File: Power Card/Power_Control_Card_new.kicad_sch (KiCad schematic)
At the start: 20 parts, among them J4 Conn_01x04_Pin, Q1 IRF5305PbF, Q2 IRF5305PbF, U3 TSR2-2450, U4 TSR2-2433, U5 MCP9808_MSOP

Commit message: test msg
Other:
- note removed: "PRETTY PLEASE SAVE (this is a git test)"
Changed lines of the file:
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@@
-		)
-	)
-	(text "PRETTY PLEASE SAVE (this is a git test)"
-		(exclude_from_sim no)
-		(at 36.068 17.018 0)
-		(effects
-			(font
-				(size 1.27 1.27)
-			)
 		)
 	)

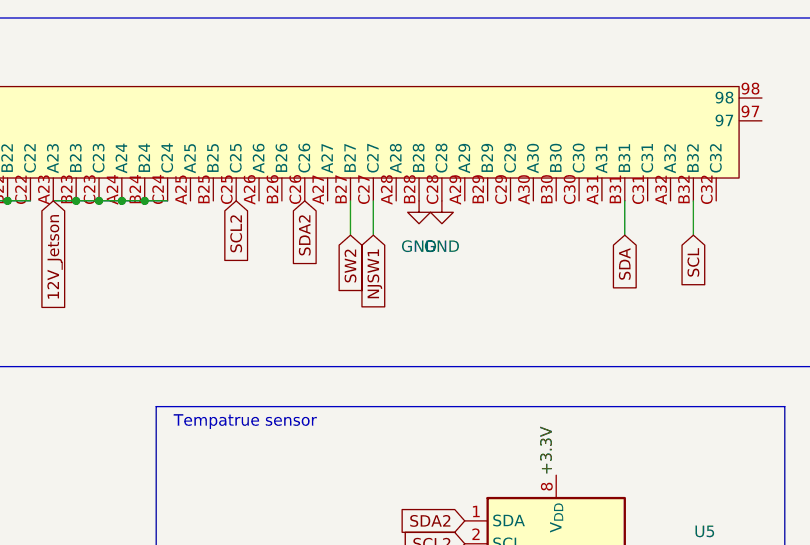
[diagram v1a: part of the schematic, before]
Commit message: Changed Backplane and Power Card for proper connection between the killswitches in the new system
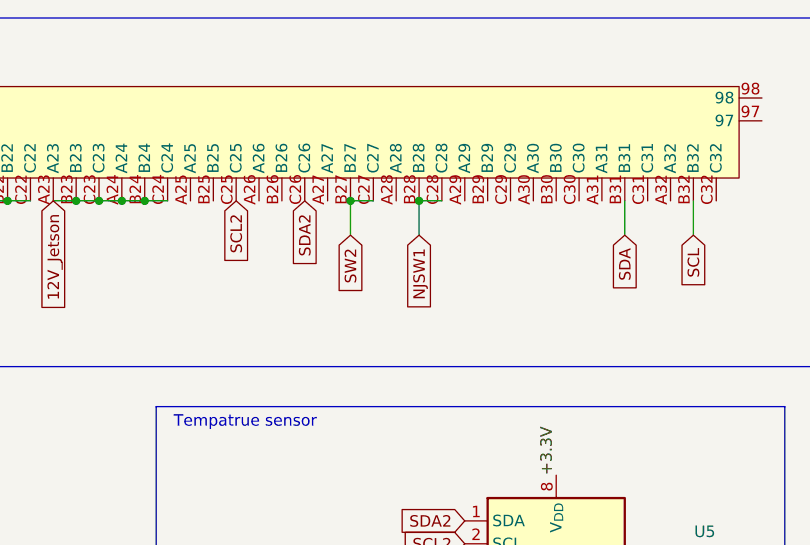
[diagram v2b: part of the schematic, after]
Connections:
- net GND: no longer J2.B28, J2.C28
- net NJSW1: now also J2.B28, J2.C28; no longer J2.C27
- net SW2: now also J2.C27
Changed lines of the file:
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@@
 	)
 	(junction
+		(at 270.51 91.44)
+		(diameter 0)
+		(color 0 0 0 0)
+	)
+	(junction
 		(at 146.05 91.44)
 		(diameter 0)
@@
 	)
 	(junction
+		(at 262.89 91.44)
+		(diameter 0)
+		(color 0 0 0 0)
+	)
+	(junction
 		(at 83.82 149.86)
 		(diameter 0)
@@
 	(wire
 		(pts
+			(xy 270.51 91.44) (xy 273.05 91.44)
+		)
+		(stroke
+			(width 0)
+			(type default)
+		)
+	)
+	(wire
+		(pts
 			(xy 118.11 91.44) (xy 120.65 91.44)
 		)
@@
 	(wire
 		(pts
-			(xy 152.4 177.8) (xy 152.4 173.99)
+			(xy 262.89 91.44) (xy 265.43 91.44)
 		)
 		(stroke
@@
 	(wire
 		(pts
-			(xy 82.55 91.44) (xy 85.09 91.44)
+			(xy 152.4 177.8) (xy 152.4 173.99)
 		)
 		(stroke
@@
 	(wire
 		(pts
-			(xy 176.53 91.44) (xy 179.07 91.44)
+			(xy 82.55 91.44) (xy 85.09 91.44)
 		)
 		(stroke
@@
 	(wire
 		(pts
-			(xy 107.95 91.44) (xy 110.49 91.44)
+			(xy 176.53 91.44) (xy 179.07 91.44)
 		)
 		(stroke
@@
 	(wire
 		(pts
-			(xy 152.4 185.42) (xy 152.4 195.58)
+			(xy 107.95 91.44) (xy 110.49 91.44)
 		)
 		(stroke
@@
 	(wire
 		(pts
-			(xy 170.18 133.35) (xy 172.72 133.35)
+			(xy 152.4 185.42) (xy 152.4 195.58)
 		)
 		(stroke
@@
 	(wire
 		(pts
-			(xy 265.43 91.44) (xy 265.43 95.25)
+			(xy 170.18 133.35) (xy 172.72 133.35)
 		)
 		(stroke
@@
 	(wire
 		(pts
+			(xy 270.51 91.44) (xy 270.51 95.25)
+		)
+		(stroke
+			(width 0)
+			(type default)
+		)
+	)
+	(wire
+		(pts
 			(xy 179.07 91.44) (xy 181.61 91.44)
 		)
@@
 	(global_label "NJSW1"
 		(shape input)
-		(at 265.43 95.25 270)
+		(at 270.51 95.25 270)
 		(fields_autoplaced yes)
 		(effects
@@
 		)
 		(property "Intersheetrefs" "${INTERSHEET_REFS}"
-			(at 265.43 104.4037 90)
+			(at 270.51 104.4037 90)
 			(effects
 				(font
@@
 	)
 	(symbol
-		(lib_name "GND_1")
-		(lib_id "power:GND")
-		(at 273.05 91.44 0)
-		(unit 1)
-		(exclude_from_sim no)
-		(in_bom yes)
-		(on_board yes)
-		(dnp no)
-		(fields_autoplaced yes)
-		(property "Reference" "#PWR011"
-			(at 273.05 97.79 0)
-			(effects
-				(font
-					(size 1.27 1.27)
-				)
-				(hide yes)
-			)
-		)
-		(property "Value" "GND"
-			(at 273.05 96.52 0)
-			(effects
-				(font
-					(size 1.27 1.27)
-				)
-			)
-		)
-		(property "Footprint" ""
-			(at 273.05 91.44 0)
-			(effects
-				(font
-					(size 1.27 1.27)
-				)
-				(hide yes)
-			)
-		)
-		(property "Datasheet" ""
-			(at 273.05 91.44 0)
-			(effects
-				(font
-					(size 1.27 1.27)
-				)
-				(hide yes)
-			)
-		)
-		(property "Description" "Power symbol creates a global label with name \"GND\" , ground"
-			(at 273.05 91.44 0)
-			(effects
-				(font
-					(size 1.27 1.27)
-				)
-				(hide yes)
-			)
-		)
-		(pin "1"
-		)
-		(instances
-			(project ""
-				(path "/377f47a5-9f77-4c4b-95f8-e010ccda5577"
-					(reference "#PWR011")
-					(unit 1)
-				)
-			)
-		)
-	)
-	(symbol
 		(lib_id "power:+12V")
 		(at 285.75 180.34 0)
@@
 					(unit 1)
 				)
-			)
-		)
-	)
-	(symbol
-		(lib_name "GND_1")
-		(lib_id "power:GND")
-		(at 270.51 91.44 0)
-		(unit 1)
-		(exclude_from_sim no)
-		(in_bom yes)
-		(on_board yes)
-		(dnp no)
-		(fields_autoplaced yes)
-		(property "Reference" "#PWR012"
-			(at 270.51 97.79 0)
-			(effects
-				(font
-					(size 1.27 1.27)
-				)
-				(hide yes)
-			)
-		)
-		(property "Value" "GND"
-			(at 270.51 96.52 0)
-			(effects
-				(font
-					(size 1.27 1.27)
-				)
-			)
-		)
-		(property "Footprint" ""
-			(at 270.51 91.44 0)
-			(effects
-				(font
-					(size 1.27 1.27)
-				)
-				(hide yes)
-			)
-		)
-		(property "Datasheet" ""
-			(at 270.51 91.44 0)
-			(effects
-				(font
-					(size 1.27 1.27)
-				)
-				(hide yes)
-			)
-		)
-		(property "Description" "Power symbol creates a global label with name \"GND\" , ground"
-			(at 270.51 91.44 0)
-			(effects
-				(font
-					(size 1.27 1.27)
-				)
-				(hide yes)
-			)
-		)
-		(pin "1"
-		)
-		(instances
-			(project "Power_Control_Card_new"
-				(path "/377f47a5-9f77-4c4b-95f8-e010ccda5577"
-					(reference "#PWR012")
-					(unit 1)
-				)
